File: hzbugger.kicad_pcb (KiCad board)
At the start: 2 copper layers, 55.4 x 26.7 mm, 54 parts, among them J2 IDC, J4 SWD, J6 GPIO, SW1 RESET_SW, SW2 BOOT0_SW, U1 STM32F103C8T6, U2 SRV05-4, U3 AMS1117-3.3, U4 HX AM 90D, Y1 8M

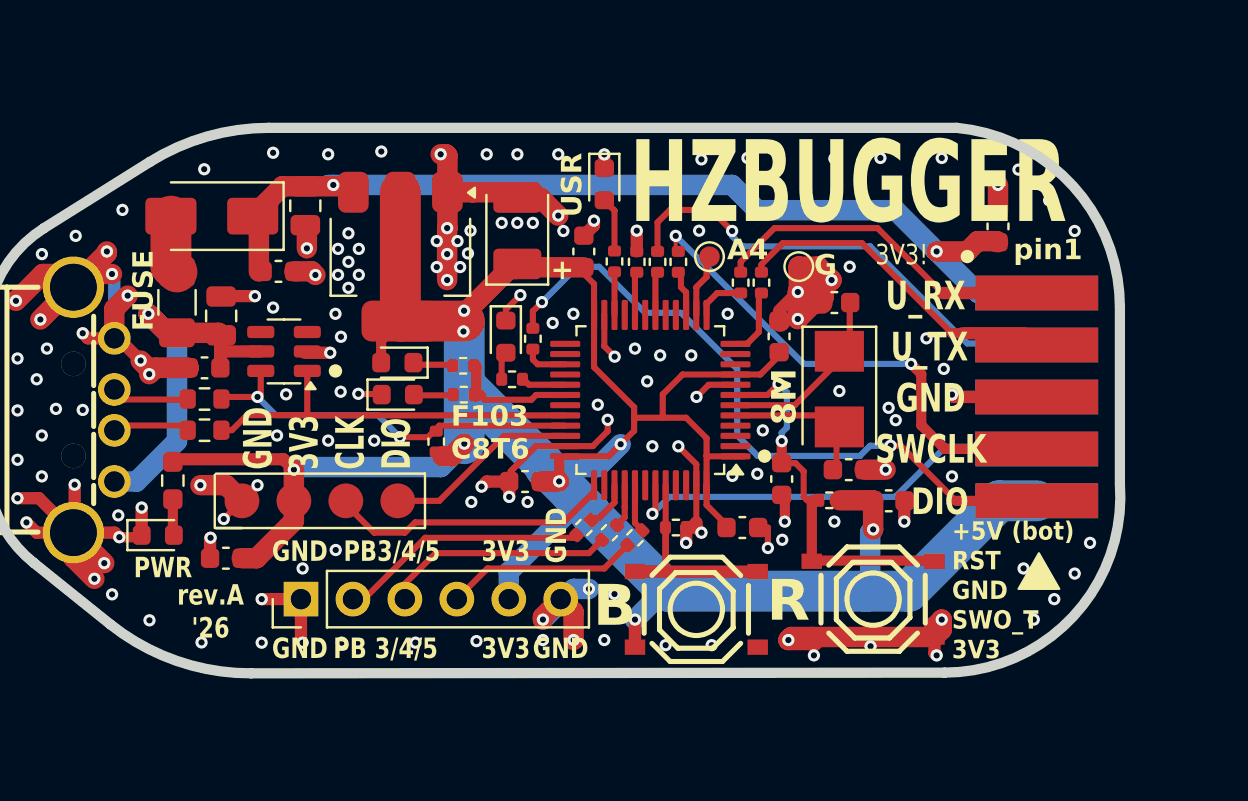
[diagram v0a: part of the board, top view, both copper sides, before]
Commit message: IDC pad lengths
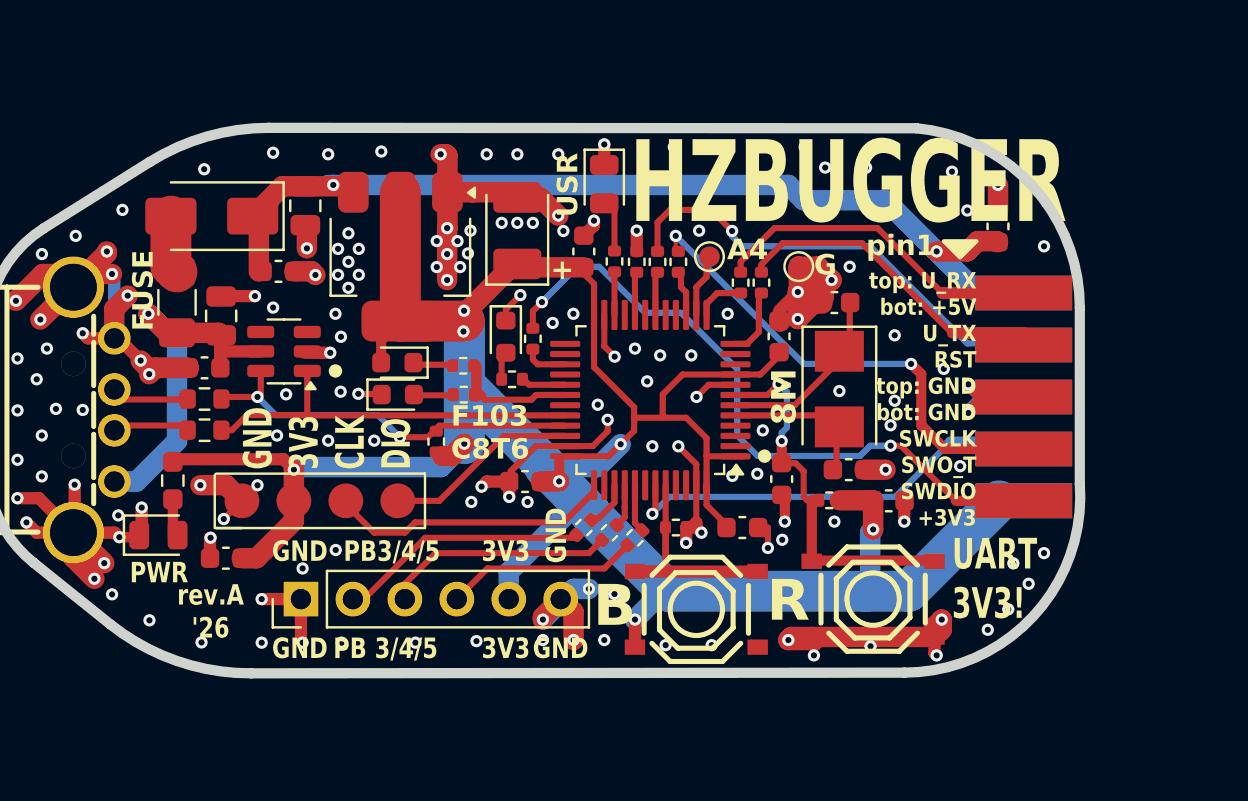
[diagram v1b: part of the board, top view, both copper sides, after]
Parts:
- D1, D6: footprint LED_SMD:LED_0603_1608Metric -> LED_SMD:LED_0805_2012Metric
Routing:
- net GND: track 140.0 -> 145.5 mm, vias 156 -> 158
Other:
- board size 55.4 x 26.7 mm -> 53.5 x 26.7 mm
- board text added: "UART 3V3!"
- board text added: "top: U_RX bot: +5V U_TX RST top: GND bot: GND SWCLK SWO_T SWDIO +3V3"
- board text removed: "+5V (bot) RST GND SWO_T 3V3"
- board text removed: "3V3!"
- board text removed: "DIO"
- board text removed: "SWCLK"
- board text removed: "U_RX"
- board text removed: "U_TX"

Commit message: silks
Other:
- board text added: "SWCLK"
- board text added: "SWDIO"
- board text added: "U_TX"
- board text added: "bot: +5V RST GND SWO_T +3V3"
- board text added: "top: U_RX"
- board text added: "top: U_RX U_TX top: GND SWCLK SWDIO"
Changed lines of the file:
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@@
 	(gr_poly
 		(pts
-			(xy 147.6 79) (xy 149.2 79) (xy 148.4 79.8)
+			(xy 147.6 78.6) (xy 149.2 78.6) (xy 148.4 79.4)
 		)
 		(stroke
@@
 		(layer "Edge.Cuts")
 	)
+	(gr_text "U_TX"
+		(at 149.2 83.8 0)
+		(layer "F.SilkS" knockout)
+		(effects
+			(font
+				(size 0.85 0.7)
+				(thickness 0.175)
+				(bold yes)
+			)
+			(justify right bottom)
+		)
+	)
 	(gr_text "pin1"
-		(at 143.8 79.8 0)
+		(at 143.8 79.4 0)
 		(layer "F.SilkS")
 		(effects
@@
 	)
 	(gr_text "UART\n3V3!"
-		(at 148 97.6 0)
+		(at 148 97.4 0)
 		(layer "F.SilkS" knockout)
 		(effects
 			(font
-				(size 1.5 1)
+				(size 1.3 1)
 				(thickness 0.25)
 				(bold yes)
@@
 		)
 	)
+	(gr_text "SWCLK"
+		(at 149.2 89.4 0)
+		(layer "F.SilkS" knockout)
+		(effects
+			(font
+				(size 0.85 0.7)
+				(thickness 0.175)
+				(bold yes)
+			)
+			(justify right bottom)
+		)
+	)
 	(gr_text "8M"
 		(at 140.5 88 90)
@@
 		)
 	)
+	(gr_text "bot: +5V\n\nRST\n\nGND\n\nSWO_T\n\n+3V3"
+		(at 149.2 93.4 0)
+		(layer "F.SilkS")
+		(effects
+			(font
+				(size 0.85 0.7)
+				(thickness 0.175)
+				(bold yes)
+			)
+			(justify right bottom)
+		)
+	)
 	(gr_text "GND"
 		(at 114.75 99.5 0)
@@
 		)
 	)
+	(gr_text "GND"
+		(at 149.2 86.6 0)
+		(layer "F.SilkS" knockout)
+		(effects
+			(font
+				(size 0.85 0.7)
+				(thickness 0.175)
+				(bold yes)
+			)
+			(justify right bottom)
+		)
+	)
 	(gr_text "B"
 		(at 131.5 98 0)
@@
 		)
 	)
+	(gr_text "top: U_RX"
+		(at 149.2 81 0)
+		(layer "F.SilkS" knockout)
+		(effects
+			(font
+				(size 0.85 0.7)
+				(thickness 0.175)
+				(bold yes)
+			)
+			(justify right bottom)
+		)
+	)
+	(gr_text "SWDIO"
+		(at 149.2 92 0)
+		(layer "F.SilkS" knockout)
+		(effects
+			(font
+				(size 0.85 0.7)
+				(thickness 0.175)
+				(bold yes)
+			)
+			(justify right bottom)
+		)
+	)
+	(gr_text "top: U_RX\n\nU_TX\n\ntop: GND\n\nSWCLK\n\nSWDIO"
+		(at 166.8 97.4 0)
+		(layer "F.SilkS" knockout)
+		(effects
+			(font
+				(size 0.85 0.7)
+				(thickness 0.175)
+				(bold yes)
+			)
+			(justify right bottom)
+		)
+	)
 	(gr_text "GND\n3V3\nCLK\nDIO"
 		(at 121.666 90.17 90)
@@
 	)
 	(gr_text "top: U_RX\nbot: +5V\nU_TX\nRST\ntop: GND\nbot: GND\nSWCLK\nSWO_T\nSWDIO\n+3V3"
-		(at 149.2 93 0)
+		(at 185.2 97.4 0)
 		(layer "F.SilkS")
 		(effects
 			(font
-				(size 0.8 0.7)
+				(size 0.85 0.7)
 				(thickness 0.175)
 				(bold yes)
@@
 	)
 	(segment
+		(start 149.414 86.614)
+		(end 152.146 86.614)
+		(width 0.6)
+		(layer "F.Cu")
+		(net 9)
+	)
+	(segment
 		(start 139.6746 91.4022)
 		(end 139.827 91.5546)
@@
 	)
 	(segment
-		(start 149.414 86.614)
-		(end 152.146 86.614)
+		(start 148.893 87.307)
+		(end 149.586 86.614)
 		(width 0.6)
 		(layer "F.Cu")
@@
 	)
 	(segment
+		(start 148.8 86)
+		(end 149.414 86.614)
+		(width 0.6)
+		(layer "F.Cu")
+		(net 9)
+	)
+	(segment
 		(start 116.3464 84.455)
 		(end 117.602 84.455)
@@
 	)
 	(segment
+		(start 149.586 86.614)
+		(end 151.511 86.614)
+		(width 0.6)
+		(layer "F.Cu")
+		(net 9)
+	)
+	(segment
 		(start 107.696 81.661)
 		(end 107.045 82.312)
@@
 	)
 	(segment
-		(start 149.586 86.614)
-		(end 148.8 87.4)
-		(width 0.6)
-		(layer "F.Cu")
-		(net 9)
-	)
-	(segment
 		(start 102.308133 91.566448)
 		(end 103.362448 91.566448)
@@
 	)
 	(segment
-		(start 148.8 86)
-		(end 149.414 86.614)
-		(width 0.6)
-		(layer "F.Cu")
-		(net 9)
-	)
-	(segment
 		(start 107.2896 93.472)
 		(end 108.48335 93.472)
@@
 	)
 	(segment
+		(start 148.8 87.307)
+		(end 148.893 87.307)
+		(width 0.6)
+		(layer "F.Cu")
+		(net 9)
+	)
+	(segment
 		(start 126.4282 90.2462)
 		(end 126.4282 90.6738)
@@
 	)
 	(segment
-		(start 151.511 86.614)
-		(end 149.586 86.614)
-		(width 0.6)
-		(layer "F.Cu")
-		(net 9)
-	)
-	(segment
 		(start 147.145 98.35)
 		(end 147.145 99.145)
@@
 	)
 	(via
-		(at 148.8 87.4)
+		(at 148.8 87.307)
 		(size 0.6)
 		(drill 0.3)
@@
 	)
 	(segment
-		(start 107.045 80.719289)
-		(end 106.930153 80.604442)
+		(start 148.8 87.307)
+		(end 149.493 86.614)
 		(width 0.6)
 		(layer "B.Cu")
@@
 	)
 	(segment
-		(start 128 97.5)
-		(end 129.5 96)
-		(width 1)
-		(layer "B.Cu")
-		(net 9)
-	)
-	(segment
-		(start 148.8 87.307)
-		(end 149.493 86.614)
+		(start 149.493 86.614)
+		(end 151.511 86.614)
 		(width 0.6)
 		(layer "B.Cu")
@@
 	)
 	(segment
-		(start 107.045 81.75)
-		(end 107.607 81.75)
+		(start 107.045 80.719289)
+		(end 106.930153 80.604442)
 		(width 0.6)
 		(layer "B.Cu")
@@
 	)
 	(segment
-		(start 148.8 87.4)
-		(end 148.8 87.307)
-		(width 0.6)
+		(start 128 97.5)
+		(end 129.5 96)
+		(width 1)
 		(layer "B.Cu")
 		(net 9)
@@
 	(segment
 		(start 107.045 81.75)
-		(end 107.045 80.719289)
+		(end 107.607 81.75)
 		(width 0.6)
 		(layer "B.Cu")
@@
 	)
 	(segment
-		(start 149.493 86.614)
-		(end 151.511 86.614)
+		(start 107.045 81.75)
+		(end 107.045 80.719289)
 		(width 0.6)
 		(layer "B.Cu")
@@
 	)
 	(segment
-		(start 148.8 86)
-		(end 149.414 86.614)
+		(start 149.414 86.614)
+		(end 152.146 86.614)
 		(width 0.6)
 		(layer "B.Cu")
@@
 	)
 	(segment
-		(start 149.414 86.614)
-		(end 152.146 86.614)
+		(start 148.8 86)
+		(end 149.414 86.614)
 		(width 0.6)
 		(layer "B.Cu")

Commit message: some final adjustments
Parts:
- moved R11 0.32 mm to (123.1, 88.8)
- moved C15 0.31 mm to (144.6, 91.7)
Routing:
- net GND: track 145.3 -> 153.1 mm
- net UART_TX: track 16.3 -> 14.9 mm
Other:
- board text added: "UART_RX"
- board text added: "UART_TX"
- board text added: "bot: +5V b: RST b: GND SWO_T b: +3V3"
- board text removed: "U_TX"
- board text removed: "bot: +5V RST GND SWO_T +3V3"
- board text removed: "top: U_RX"
- board text removed: "top: U_RX U_TX top: GND SWCLK SWDIO"
- board text removed: "top: U_RX bot: +5V U_TX RST top: GND bot: GND SWCLK SWO_T SWDIO +3V3"

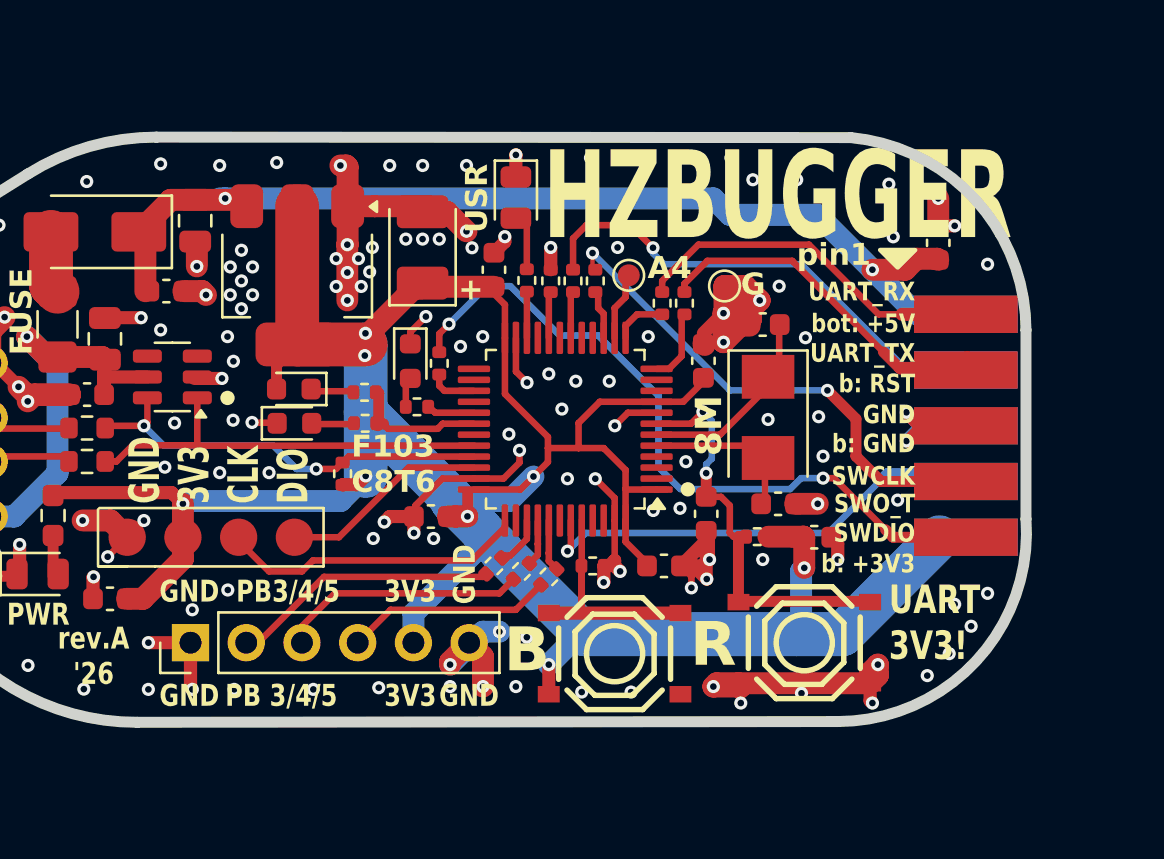
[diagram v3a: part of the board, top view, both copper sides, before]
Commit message: outline, to fit idc
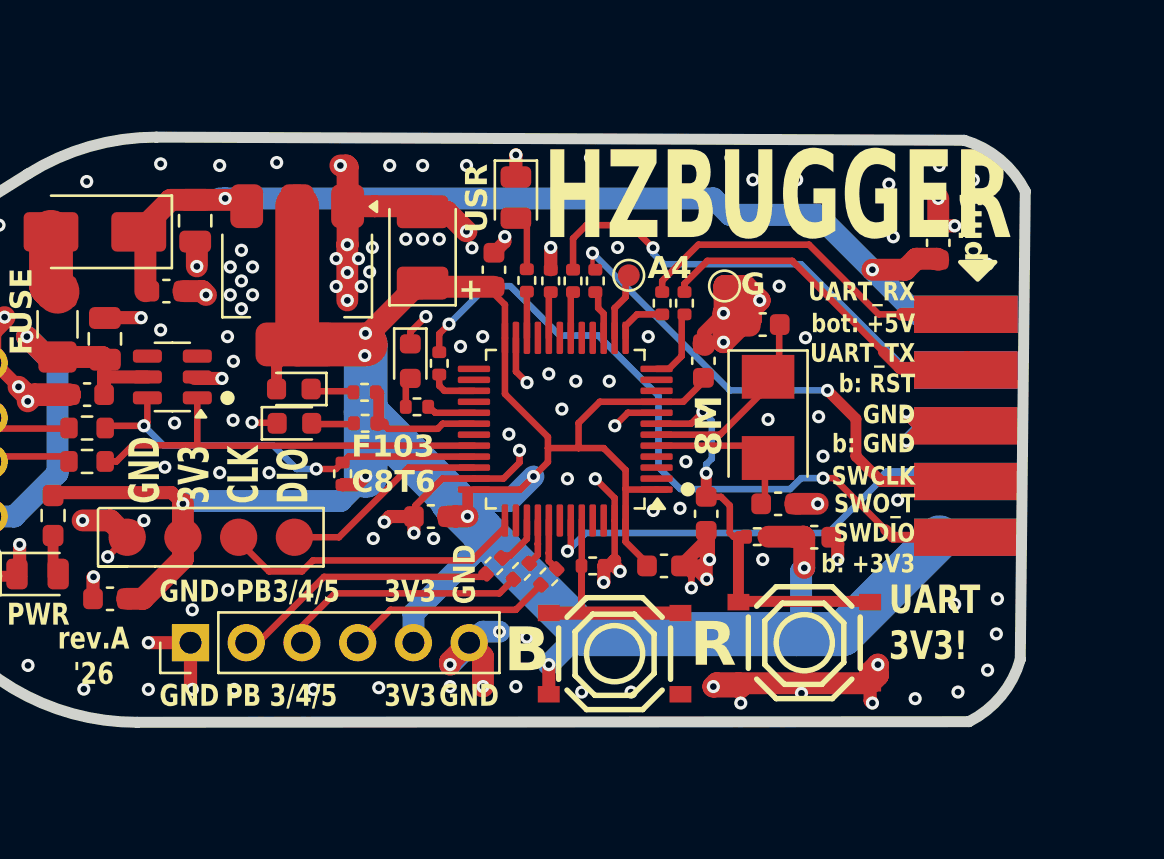
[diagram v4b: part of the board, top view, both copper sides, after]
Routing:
- net GND: vias 158 -> 162
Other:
- board size 53.5 x 26.7 mm -> 53.4 x 26.7 mm
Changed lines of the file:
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@@
 	(gr_poly
 		(pts
-			(xy 147.6 78.6) (xy 149.2 78.6) (xy 148.4 79.4)
+			(xy 151.25 79.15) (xy 152.85 79.15) (xy 152.05 79.95)
 		)
 		(stroke
@@
 	)
 	(gr_line
-		(start 114.612809 73.4568)
-		(end 146.266471 73.478247)
-		(stroke
-			(width 0.5)
-			(type default)
-		)
-		(layer "Edge.Cuts")
-	)
-	(gr_arc
-		(start 154.25 90.86573)
-		(mid 151.793601 97.529132)
-		(end 145.671133 100.094325)
+		(start 114.612809 73.456816)
+		(end 151.43717 73.600567)
 		(stroke
 			(width 0.5)
@@
 	)
 	(gr_arc
-		(start 146.27548 73.4791)
-		(mid 151.958383 76.322861)
-		(end 154.25 82.249901)
+		(start 153.989652 97.26525)
+		(mid 153.074614 98.982292)
+		(end 151.649996 100.100013)
+		(stroke
+			(width 0.5)
+			(type default)
+		)
+		(layer "Edge.Cuts")
+	)
+	(gr_arc
+		(start 151.43717 73.600567)
+		(mid 153.1 74.5)
+		(end 154.217708 75.924614)
 		(stroke
 			(width 0.5)
@@
 	)
 	(gr_line
-		(start 154.249999 90.865829)
-		(end 154.25 82.25)
+		(start 153.989652 97.26525)
+		(end 154.217708 75.924614)
 		(stroke
 			(width 0.5)
@@
 	(gr_line
 		(start 113.736517 100.128058)
-		(end 145.671133 100.094325)
+		(end 151.649996 100.100013)
 		(stroke
 			(width 0.5)
@@
 	)
 	(gr_text "pin1"
-		(at 143.8 79.4 0)
+		(at 152.35 79.15 90)
 		(layer "F.SilkS")
 		(effects
@@
 	)
 	(via
-		(at 149.75 98)
+		(at 149.2 99.05)
 		(size 0.6)
 		(drill 0.3)
@@
 	)
 	(via
+		(at 150.3 74.75)
+		(size 0.6)
+		(drill 0.3)
+		(layers "F.Cu" "B.Cu")
+		(free yes)
+		(net 9)
+	)
+	(via
 		(at 127.508 78.105)
 		(size 0.6)
@@
 	)
 	(via
+		(at 152.9 96.1)
+		(size 0.6)
+		(drill 0.3)
+		(layers "F.Cu" "B.Cu")
+		(free yes)
+		(net 9)
+	)
+	(via
 		(at 114.808 74.676)
 		(size 0.6)
@@
 	)
 	(via
-		(at 150.75 97)
+		(at 151.15 98.75)
+		(size 0.6)
+		(drill 0.3)
+		(layers "F.Cu" "B.Cu")
+		(free yes)
+		(net 9)
+	)
+	(via
+		(at 152.85 76.9)
 		(size 0.6)
 		(drill 0.3)
@@
 	)
 	(via
-		(at 152.5 94.25)
+		(at 152.95 94.5)
 		(size 0.6)
 		(drill 0.3)
@@
 	)
 	(via
-		(at 151.75 95.75)
+		(at 152.5 97.75)
 		(size 0.6)
 		(drill 0.3)
@@
 		(size 0.6)
 		(drill 0.3)
+		(layers "F.Cu" "B.Cu")
+		(free yes)
+		(net 9)
+	)
+	(via
+		(at 151.85 75.4)
+		(size 0.6)
+		(drill 0.3)

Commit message: cap
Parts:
- moved C16 0.64 mm to (137.2, 92.6), turned to -90 degrees
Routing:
- net GND: track 153.1 -> 152.4 mm, vias 162 -> 164
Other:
- board size 53.4 x 26.7 mm -> 53.5 x 26.7 mm

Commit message: tx led
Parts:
- added D7: LED1, LED_SMD:LED_0603_1608Metric, F.Cu at (141.8, 80.2)
- added R20: 1k5, Resistor_SMD:R_0402_1005Metric, F.Cu at (144.0, 80.2)
- R11: footprint Resistor_SMD:R_0402_1005Metric -> Resistor_SMD:R_0402_1005Metric_Pad0.72x0.64mm_HandSolder
- moved TP2 6.92 mm to (135.2, 75.8)
- moved D6 1.06 mm to (132.1, 76.2), turned to 180 degrees
- moved C11 0.40 mm to (142.6, 82.2), turned to 180 degrees
- moved R11 0.23 mm to (123.2, 89.0)
- moved J4 0.08 mm to (113.2, 91.7)
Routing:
- net GND: track 152.4 -> 145.3 mm, vias 164 -> 163
- net +3V3: track 142.9 -> 148.1 mm
- net UART_TX: track 14.9 -> 13.3 mm
- net Net-(D7-K): track 0.00 -> 1.60 mm
- net Net-(D6-A): track 2.69 -> 3.44 mm
- net UART_RX: track 17.0 -> 16.3 mm
- net Net-(U1-PD1): track 9.04 -> 9.61 mm
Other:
- board text added: "USR1"
- board text added: "USR2"
- board text added: "uTX"
- board text removed: "G"
- board text removed: "USR"
